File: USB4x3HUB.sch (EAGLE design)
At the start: 111 parts, among them IC1 TUSB2036, IC10 SN74LVC1G139DCUR, IC2 FSUSB74MPX, IC6 3.3V, IC7 5V, IC8 5V, IC9 5V, Q1 OSC4_6.0M, SW1 RD, SW2 BL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

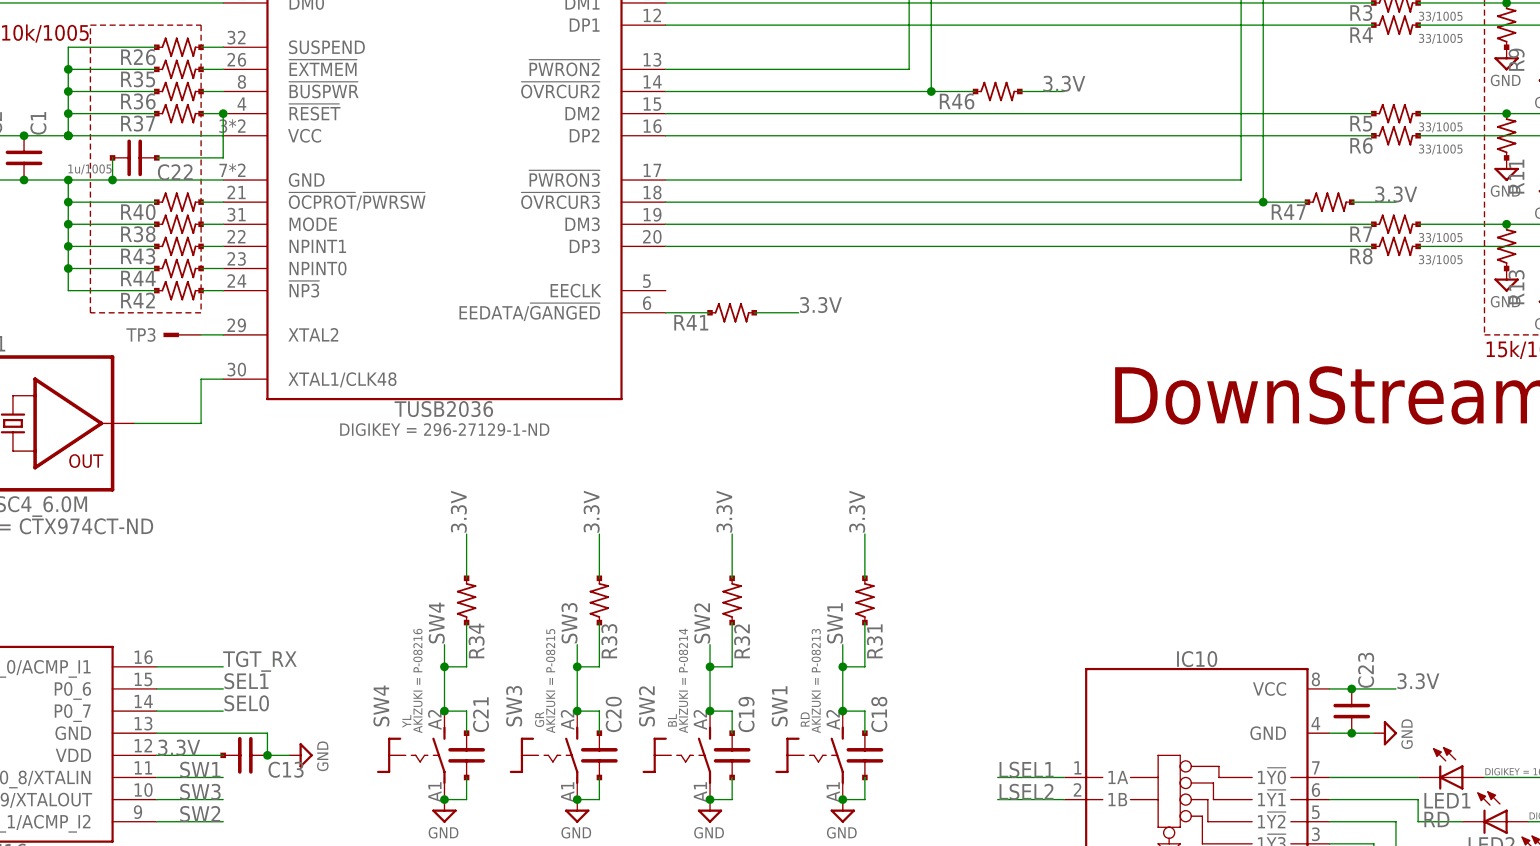
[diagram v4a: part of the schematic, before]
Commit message: some trace width wider 0.2 -> 0.25mm; Capacotors re-numbering
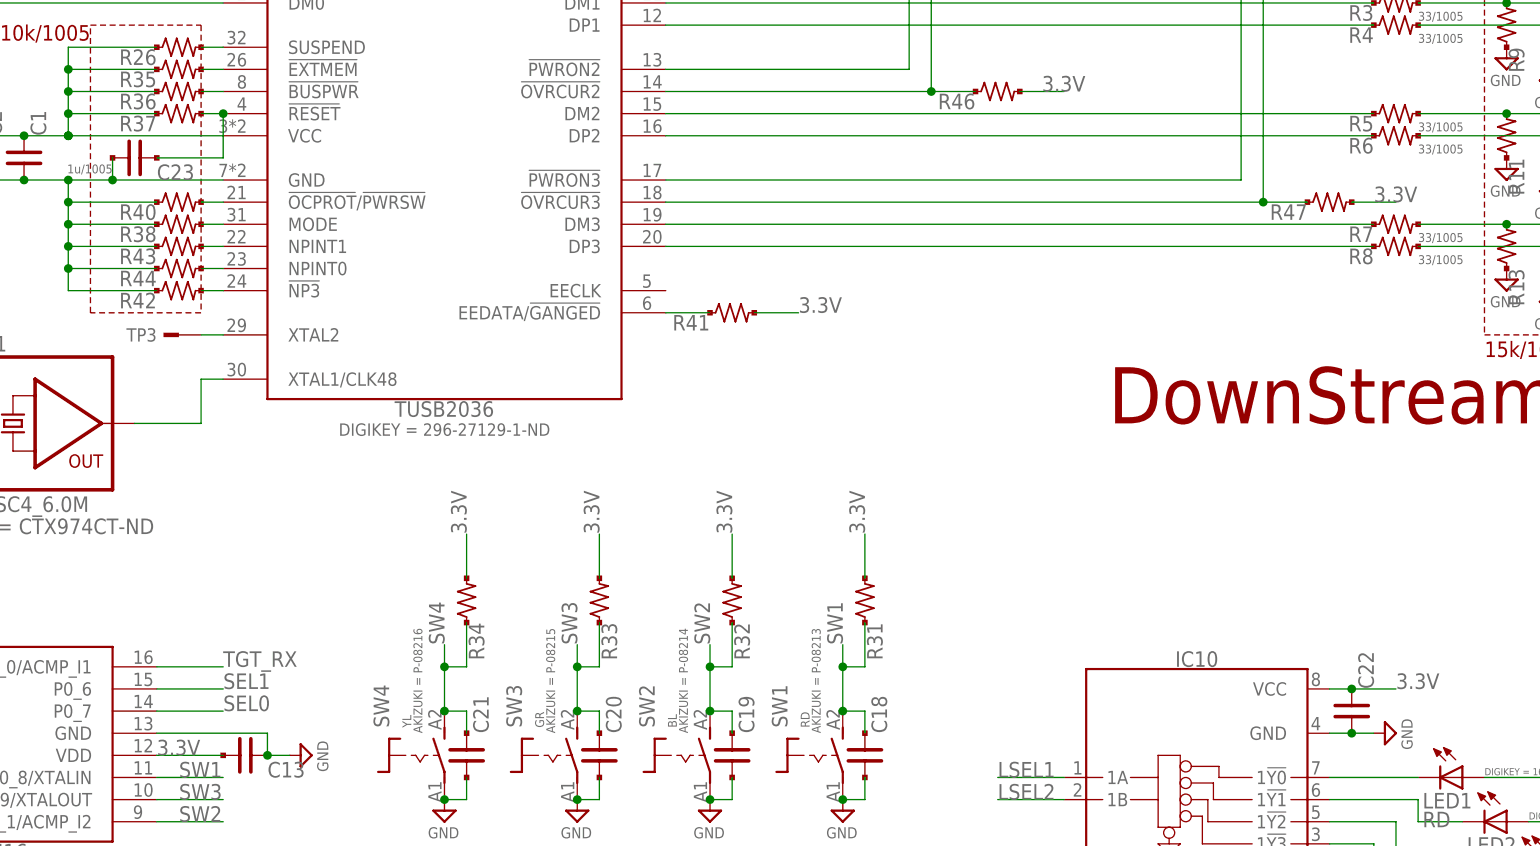
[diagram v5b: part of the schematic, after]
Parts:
- C22: value 1u/1005 -> (none); device mylib:C_SMD_1.0U_1005 -> mylib:C_SMD_0.1U_1005
- C23: value (none) -> 1u/1005; device mylib:C_SMD_0.1U_1005 -> mylib:C_SMD_1.0U_1005
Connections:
- net 3.3V: now also C22.1; no longer C23.1
- net N$62: now also C23.1; no longer C22.1
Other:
- moved on the sheet: C22, C23
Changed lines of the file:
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@@
 <part name="R26" library="mylib" deviceset="R_US_*" device="_1005" technology="10K"/>
 <part name="IC10" library="mylib" deviceset="IC_TTL_SINGLE_74_139" device="_FLAT" value=" SN74LVC1G139DCUR"/>
-<part name="C23" library="mylib" deviceset="C_SMD_*" device="_1005" technology="0.1U"/>
+<part name="C22" library="mylib" deviceset="C_SMD_*" device="_1005" technology="0.1U"/>
 <part name="SUPPLY33" library="mylib" deviceset="GND" device=""/>
 <part name="LED1" library="led_local" deviceset="LED" device="CHIPLED_0805" technology="RD" value="RD"/>
@@
 <part name="SUPPLY38" library="mylib" deviceset="GND" device=""/>
 <part name="SUPPLY39" library="mylib" deviceset="GND" device=""/>
-<part name="C22" library="mylib" deviceset="C_SMD_*" device="_1005" technology="1.0U" value="1u/1005"/>
+<part name="C23" library="mylib" deviceset="C_SMD_*" device="_1005" technology="1.0U" value="1u/1005"/>
 <part name="TP4" library="mylib" deviceset="TESTPAD" device=""/>
 <part name="R45" library="mylib" deviceset="R_US_*" device="_1005" technology="10K"/>
@@
 <attribute name="DIGIKEY" x="284.48" y="60.96" size="1.016" layer="96" align="top-center" display="both"/>
 </instance>
-<instance part="C23" gate="G$1" x="302.26" y="81.28"/>
+<instance part="C22" gate="G$1" x="302.26" y="81.28"/>
 <instance part="SUPPLY33" gate="GND" x="307.34" y="78.74" rot="R90"/>
 <instance part="LED1" gate="G$1" x="314.96" y="73.66" rot="R270">
@@
 <instance part="SUPPLY38" gate="GND" x="43.18" y="134.62" rot="R90"/>
 <instance part="SUPPLY39" gate="GND" x="43.18" y="109.22" rot="R90"/>
-<instance part="C22" gate="G$1" x="162.56" y="144.78" rot="R270"/>
+<instance part="C23" gate="G$1" x="162.56" y="144.78" rot="R270"/>
 <instance part="TP4" gate="1" x="109.22" y="71.12" rot="R180"/>
 <instance part="R45" gate="G$1" x="236.22" y="165.1"/>
@@
 <pinref part="R44" gate="G$1" pin="1"/>
 <pinref part="R42" gate="G$1" pin="1"/>
-<pinref part="C22" gate="G$1" pin="2"/>
+<pinref part="C23" gate="G$1" pin="2"/>
 <wire x1="160.02" y1="144.78" x2="160.02" y2="142.24" width="0.1524" layer="91"/>
 <junction x="160.02" y="142.24"/>
@@
 <segment>
 <pinref part="IC10" gate="G$1" pin="GND"/>
-<pinref part="C23" gate="G$1" pin="2"/>
+<pinref part="C22" gate="G$1" pin="2"/>
 <pinref part="SUPPLY33" gate="GND" pin="GND"/>
 <wire x1="302.26" y1="78.74" x2="299.72" y2="78.74" width="0.1524" layer="91"/>
@@
 <wire x1="302.26" y1="83.82" x2="307.34" y2="83.82" width="0.1524" layer="91"/>
 <pinref part="IC10" gate="G$1" pin="VCC"/>
-<pinref part="C23" gate="G$1" pin="1"/>
+<pinref part="C22" gate="G$1" pin="1"/>
 <wire x1="302.26" y1="83.82" x2="299.72" y2="83.82" width="0.1524" layer="91"/>
 <junction x="302.26" y="83.82"/>
@@
 <pinref part="IC1" gate="G$1" pin="!RESET!"/>
 <pinref part="R37" gate="G$1" pin="2"/>
-<pinref part="C22" gate="G$1" pin="1"/>
+<pinref part="C23" gate="G$1" pin="1"/>
 <wire x1="170.18" y1="149.86" x2="172.72" y2="149.86" width="0.1524" layer="91"/>
 <junction x="172.72" y="149.86"/>

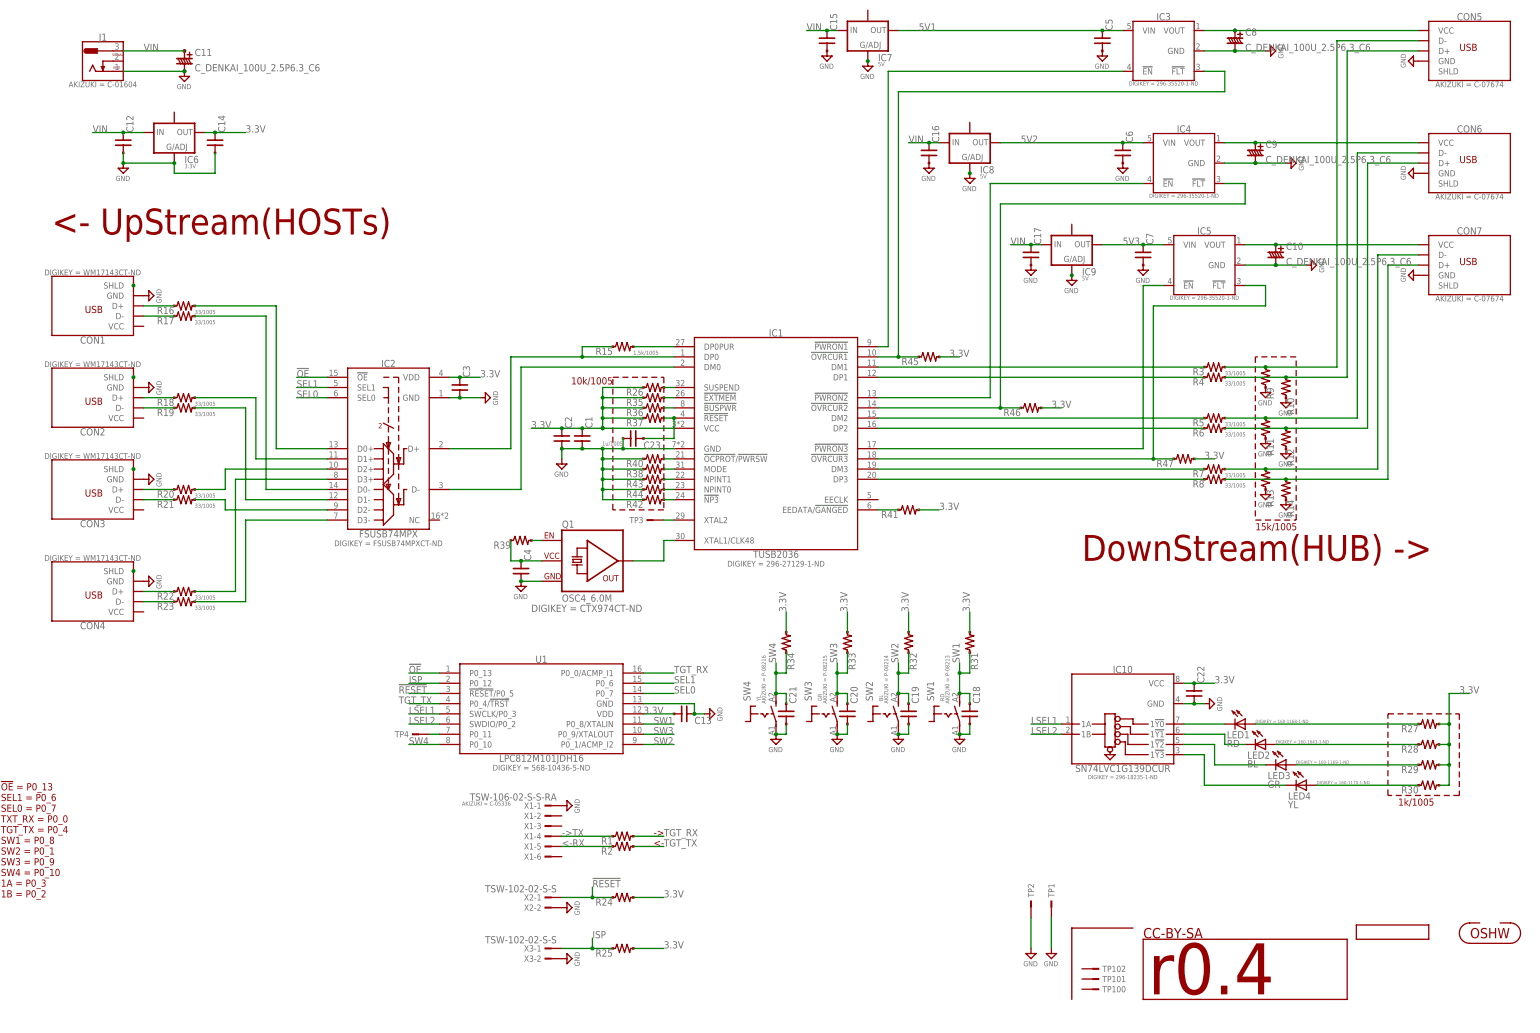
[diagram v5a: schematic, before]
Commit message: IC6/R16-23,31-34,36,37,41/C1,12,14,18-23 move; LED1-4 colors
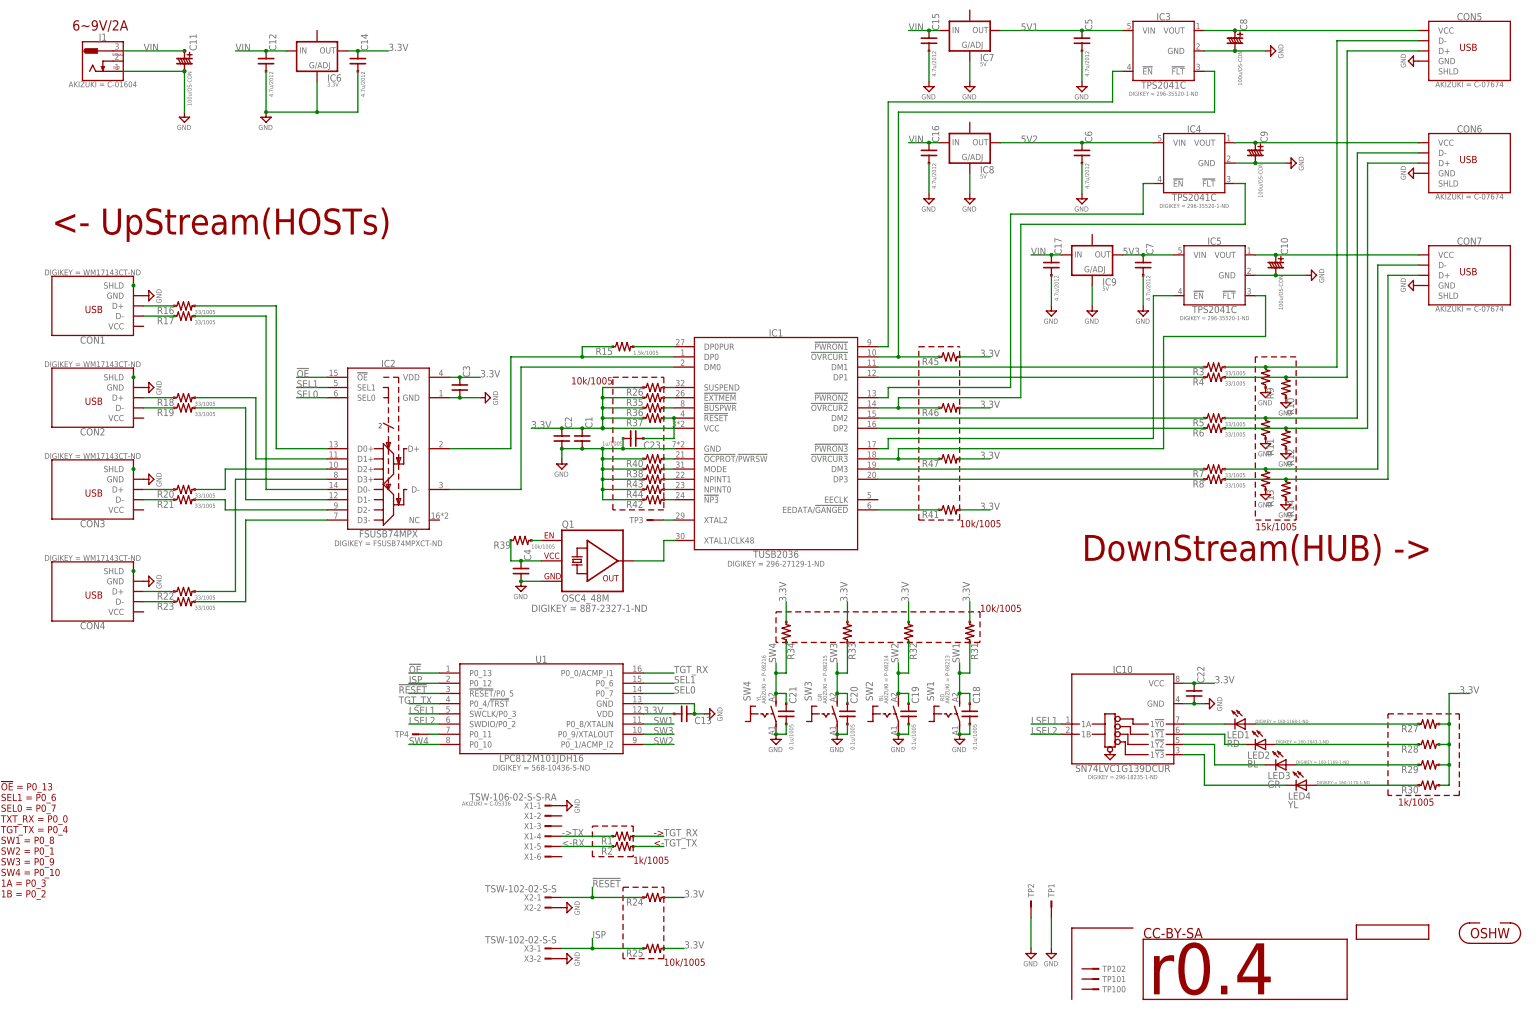
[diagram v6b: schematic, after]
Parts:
- C10, C11, C8, C9: value C_DENKAI_100U_2.5P6.3_C6 -> 100u/OS-CON
- C12, C14, C15, C16, C17, C5, C6, C7: value (none) -> 4.7u/2012
- C18, C19, C20, C21: value (none) -> 0.1u/1005
- IC3, IC4, IC5: value (none) -> TPS2041C
- Q1: value OSC4_6.0M -> OSC4_48M; device mylib:OSC4_6.0M -> mylib:OSC4_48M
- R39: value (none) -> 10k/1005
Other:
- note added: "6~9V/2A"
- moved on the sheet: C10, C12, C14, C15, C17, C5, C6, C7, CON7, IC4, IC5, IC6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

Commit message: library update; MinLab brand;R15
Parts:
- added I1: (no value), mylib:ICON_MINLAB_5.2S
- added P1, P2, P3, P4: (no value), mylib:PCB_CORNER
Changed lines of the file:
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@@
 <part name="SUPPLY40" library="mylib" deviceset="GND" device=""/>
 <part name="SUPPLY41" library="mylib" deviceset="GND" device=""/>
+<part name="I1" library="mylib" deviceset="ICON_MINLAB" device="_5.2S"/>
+<part name="P1" library="mylib" deviceset="PCB_CORNER" device=""/>
+<part name="P2" library="mylib" deviceset="PCB_CORNER" device=""/>
+<part name="P3" library="mylib" deviceset="PCB_CORNER" device=""/>
+<part name="P4" library="mylib" deviceset="PCB_CORNER" device=""/>
 </parts>
 <sheets>
@@
 <text x="167.64" y="43.18" size="1.778" layer="94">&lt;-</text>
 <text x="167.64" y="45.72" size="1.778" layer="94">-&gt;</text>
-<text x="5.08" y="30.48" size="1.778" layer="94">!OE! = P0_13
+<text x="76.2" y="60.96" size="1.778" layer="94">!OE! = P0_13
 SEL1 = P0_6
 SEL0 = P0_7
@@
 <wire x1="248.92" y1="93.98" x2="198.12" y2="93.98" width="0.1524" layer="94" style="shortdash"/>
 <text x="243.84" y="124.46" size="1.778" layer="94" rot="R180" align="bottom-right">10k/1005</text>
+<wire x1="241.3" y1="17.78" x2="241.3" y2="10.16" width="0.3048" layer="94"/>
+<wire x1="246.38" y1="5.08" x2="251.46" y2="5.08" width="0.3048" layer="94"/>
+<wire x1="256.54" y1="10.16" x2="256.54" y2="17.78" width="0.3048" layer="94"/>
+<wire x1="251.46" y1="22.86" x2="246.38" y2="22.86" width="0.3048" layer="94"/>
 </plain>
 <instances>
@@
 <instance part="SUPPLY40" gate="GND" x="355.6" y="210.82" rot="R270"/>
 <instance part="SUPPLY41" gate="GND" x="355.6" y="182.88" rot="R270"/>
+<instance part="I1" gate="G$1" x="370.84" y="25.4"/>
+<instance part="P1" gate="G$1" x="251.46" y="17.78"/>
+<instance part="P2" gate="G$1" x="246.38" y="17.78" rot="R90"/>
+<instance part="P3" gate="G$1" x="246.38" y="10.16" rot="R180"/>
+<instance part="P4" gate="G$1" x="251.46" y="10.16" rot="R270"/>
 </instances>
 <busses>

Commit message: [ NEW ] r04 PCB pic
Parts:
- GIT1: value (none) -> 71cae1b
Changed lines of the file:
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@@
 <part name="ICON1" library="mylib" deviceset="ICON_OSHW" device="" value="OSHW"/>
 <part name="ICON2" library="mylib" deviceset="ICON_REVISION" device="_2.0" value="r0.4"/>
-<part name="GIT1" library="git-revision" deviceset="GIT-REVISION" device=""/>
+<part name="GIT1" library="git-revision" deviceset="GIT-REVISION" device="" value="71cae1b"/>
 <part name="TP1" library="mylib" deviceset="TESTPAD" device="_4020"/>
 <part name="TP2" library="mylib" deviceset="TESTPAD" device="_4020"/>
